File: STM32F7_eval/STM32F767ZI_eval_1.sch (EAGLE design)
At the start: 101 parts, among them CN3 GROVE-4P-CONN-I2C-90D, CN4 GROVE-4P-CONN-AN01-90D, CN5 ARDUINO_COMPAT_IF, CN6 STLINKV21_SWD_IF, CN7 WFT0750CZ09-SMD_, CN8 MCO_IF, CN9 UART_IF, Q1 PMF370XN_, SW1 SKRPACE010_, SW2 SKRPACE010_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

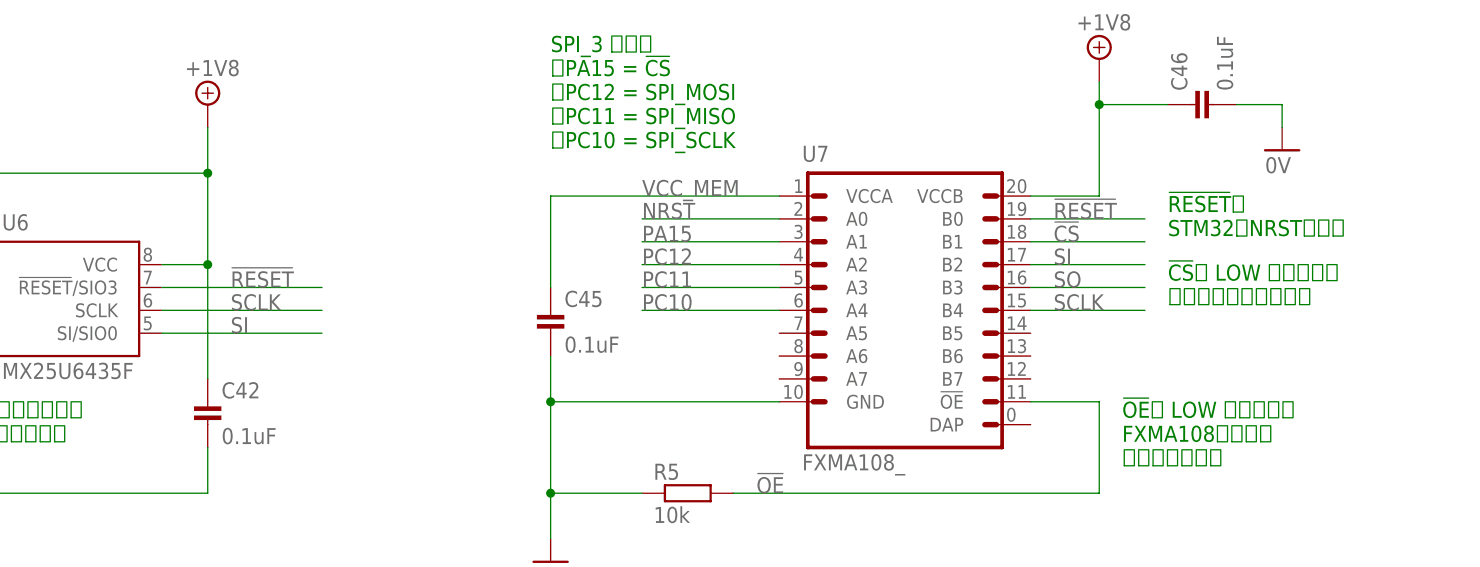
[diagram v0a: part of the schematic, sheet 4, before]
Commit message: 評価回路を修正
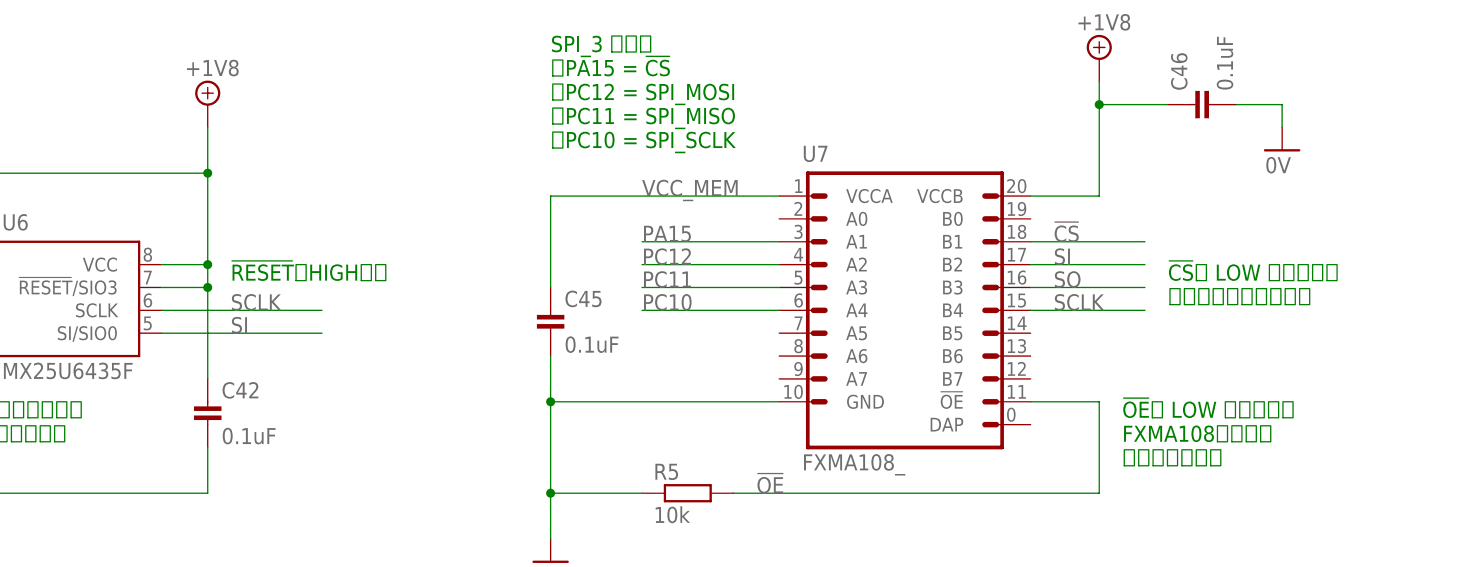
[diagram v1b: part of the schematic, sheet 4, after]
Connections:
- removed net !RESET!: U6.!RESET!/SIO3, U7.B0
- new net PE15: U1.PE15, U5.!RESET!
- net +1V8: now also U6.!RESET!/SIO3
- net NRST: no longer U5.!RESET!, U7.A0
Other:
- note added: "!RESET!はHIGH固定"
- note removed: "!RESET!は STM32のNRSTに接続"
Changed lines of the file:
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@@
 <setting verticaltext="up"/>
 </settings>
-<grid distance="0.1" unitdist="inch" unit="inch" style="lines" multiple="1" display="no" altdistance="0.01" altunitdist="inch" altunit="inch"/>
+<grid distance="0.1" unitdist="inch" unit="inch" style="lines" multiple="1" display="yes" altdistance="0.01" altunitdist="inch" altunit="inch"/>
 <layers>
 <layer number="1" name="Top" color="4" fill="1" visible="no" active="no"/>
@@
 <net name="NRST" class="0">
 <segment>
-<pinref part="U1" gate="G$1" pin="NRST"/>
-<wire x1="129.54" y1="139.7" x2="119.38" y2="139.7" width="0.1524" layer="91"/>
-<label x="121.92" y="139.7" size="1.778" layer="95"/>
-</segment>
-<segment>
 <pinref part="C17" gate="G$1" pin="1"/>
 <wire x1="232.41" y1="35.56" x2="226.06" y2="35.56" width="0.1524" layer="91"/>
@@
 <junction x="226.06" y="45.72"/>
 <label x="215.9" y="45.72" size="1.778" layer="95"/>
+</segment>
+<segment>
+<pinref part="U1" gate="G$1" pin="NRST"/>
+<wire x1="129.54" y1="139.7" x2="119.38" y2="139.7" width="0.1524" layer="91"/>
+<label x="121.92" y="139.7" size="1.778" layer="95"/>
 </segment>
 </net>
@@
 <wire x1="22.86" y1="142.24" x2="22.86" y2="154.94" width="0.1524" layer="91"/>
 <label x="22.86" y="144.78" size="1.778" layer="95" rot="R90"/>
+</segment>
+</net>
+<net name="PE15" class="0">
+<segment>
+<pinref part="U1" gate="G$1" pin="PE15"/>
+<wire x1="226.06" y1="93.98" x2="226.06" y2="83.82" width="0.1524" layer="91"/>
+<label x="226.06" y="86.36" size="1.778" layer="95" rot="R90"/>
 </segment>
 </net>
@@
 </segment>
 </net>
-<net name="NRST" class="0">
-<segment>
-<pinref part="U5" gate="G$1" pin="!RESET!"/>
-<wire x1="76.2" y1="33.02" x2="60.96" y2="33.02" width="0.1524" layer="91"/>
-<label x="63.5" y="33.02" size="1.778" layer="95"/>
-</segment>
-</net>
 <net name="PB10" class="0">
 <segment>
@@
 </segment>
 </net>
+<net name="PE15" class="0">
+<segment>
+<pinref part="U5" gate="G$1" pin="!RESET!"/>
+<wire x1="76.2" y1="33.02" x2="60.96" y2="33.02" width="0.1524" layer="91"/>
+<label x="63.5" y="33.02" size="1.778" layer="95"/>
+</segment>
+</net>
 </nets>
 </sheet>
@@
 <text x="200.66" y="76.2" size="1.778" layer="91" align="top-left">!CS!に LOW を出力時は
 フラッシュが使用可能</text>
-<text x="200.66" y="83.82" size="1.778" layer="91" align="top-left">!RESET!は
-STM32のNRSTに接続</text>
+<text x="96.52" y="76.2" size="1.778" layer="91" align="top-left">!RESET!はHIGH固定</text>
 <text x="195.58" y="60.96" size="1.778" layer="91" align="top-left">!OE!に LOW を出力時は
 FXMA108のバスが
@@
 </segment>
 </net>
-<net name="!RESET!" class="0">
-<segment>
-<pinref part="U7" gate="G$1" pin="B0"/>
-<wire x1="185.42" y1="81.28" x2="198.12" y2="81.28" width="0.1524" layer="91"/>
-<label x="187.96" y="81.28" size="1.778" layer="95"/>
-</segment>
-<segment>
-<pinref part="U6" gate="G$1" pin="!RESET!/SIO3"/>
-<wire x1="106.68" y1="73.66" x2="88.9" y2="73.66" width="0.1524" layer="91"/>
-<label x="96.52" y="73.66" size="1.778" layer="95"/>
-</segment>
-</net>
 <net name="!CS!" class="0">
 <segment>
@@
 <wire x1="106.68" y1="71.12" x2="88.9" y2="71.12" width="0.1524" layer="91"/>
 <label x="96.52" y="71.12" size="1.778" layer="95"/>
-</segment>
-</net>
-<net name="NRST" class="0">
-<segment>
-<pinref part="U7" gate="G$1" pin="A0"/>
-<wire x1="157.48" y1="81.28" x2="142.24" y2="81.28" width="0.1524" layer="91"/>
-<label x="142.24" y="81.28" size="1.778" layer="95"/>
 </segment>
 </net>
@@
 <pinref part="C42" gate="G$1" pin="1"/>
 <wire x1="93.98" y1="86.36" x2="93.98" y2="91.44" width="0.1524" layer="91"/>
-<wire x1="93.98" y1="76.2" x2="93.98" y2="63.5" width="0.1524" layer="91"/>
+<wire x1="93.98" y1="76.2" x2="93.98" y2="73.66" width="0.1524" layer="91"/>
 <junction x="93.98" y="76.2"/>
 <pinref part="SUPPLY1" gate="G$1" pin="+1V8"/>
 <pinref part="U6" gate="G$1" pin="!WP!/SIO2"/>
+<wire x1="93.98" y1="73.66" x2="93.98" y2="63.5" width="0.1524" layer="91"/>
 <wire x1="55.88" y1="71.12" x2="43.18" y2="71.12" width="0.1524" layer="91"/>
 <wire x1="43.18" y1="71.12" x2="43.18" y2="86.36" width="0.1524" layer="91"/>
 <wire x1="43.18" y1="86.36" x2="93.98" y2="86.36" width="0.1524" layer="91"/>
 <junction x="93.98" y="86.36"/>
-</segment>
-<segment>
+<pinref part="U6" gate="G$1" pin="!RESET!/SIO3"/>
+<wire x1="88.9" y1="73.66" x2="93.98" y2="73.66" width="0.1524" layer="91"/>
+<junction x="93.98" y="73.66"/>
+</segment>
+<segment>

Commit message: 回路図を修正
・部品のパッケージを入れ替え
・セキュリティーチップ回路図のシートを移動
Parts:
- removed C28: 0.1uF, Parts:CAP_0603_DEV
- removed C29: 10uF, Parts:CAP_0805_DEV
- removed CN8: MCO_IF, PartsForProto:MCO_IF
- removed R19, R20: 3.3k, Parts:RESISTOR_0603_DEV
- removed R26: 0, Parts:RESISTOR_0603_DEV
- removed U5: STSAFE, Parts:STSAFE
- added C47: 0.1uF, Parts:CAP_0603_DEV
- added C48: 10uF, Parts:CAP_0805_DEV
- added R27, R28: 3.3k, Parts:RESISTOR_0603_DEV
- added R29: 0, Parts:RESISTOR_0603_DEV
- added U9: STSAFE, Parts:STSAFE
- CN4: value GROVE-4P-CONN-AN01-90D -> GROVE-4P-CONN-I2C-90D; device PartsForProto:GROVE-4P-CONN-AN01-90D -> PartsForProto:GROVE-4P-CONN-I2C-90D
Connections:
- net 0V: now also C47.2, C48.2, CN4.GND, U9.GND; no longer C28.2, C29.2, U5.GND
- net AGND: no longer CN4.GND
- net AVDD: no longer CN4.VCC
- net PA3: no longer CN4.A0
- net PB10: now also R27.1, U9.SCL; no longer R19.1, U5.SCL
- net PB11: now also R28.1, U9.SDA; no longer R20.1, U5.SDA
- net PB8: now also CN4.SCL
- net PB9: now also CN4.SDA
- net PC0: no longer CN4.A1
- net PE15: now also U9.!RESET!; no longer U5.!RESET!
- net PH0: no longer CN8.MCO
- net VCC_STSAFE: now also C47.1, C48.1, R27.2, R28.2, R29.1, U9.VCC; no longer C28.1, C29.1, R19.2, R20.2, R26.1, U5.VCC
- net VDD: now also CN4.VCC, R29.2; no longer R26.2
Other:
- note added: "Groveコネクター ・I2Cポート x 2"
- note added: "実装していません"
- note removed: "Groveコネクター ・I2Cポート ・アナログポート"
- note removed: "ST-LINK V2-1からの マスタークロック入力ピン"

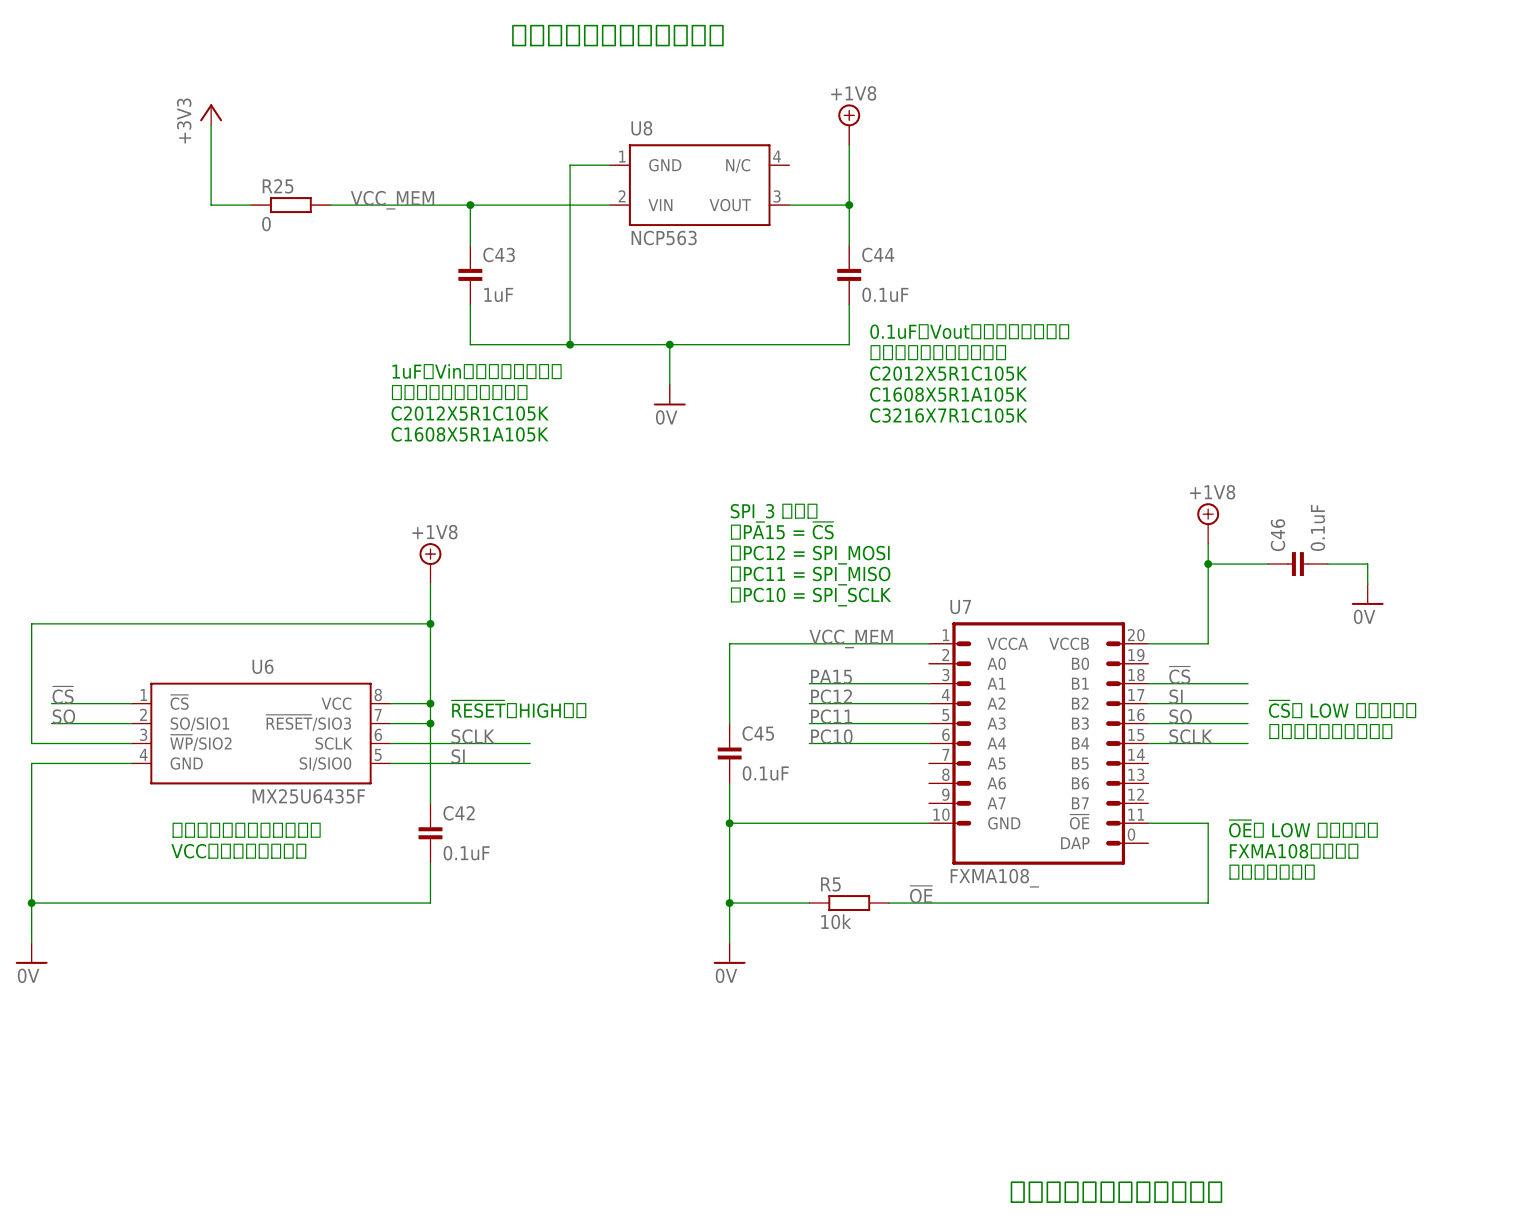
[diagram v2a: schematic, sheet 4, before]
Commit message: 回路図を修正
・構成部品を入替え
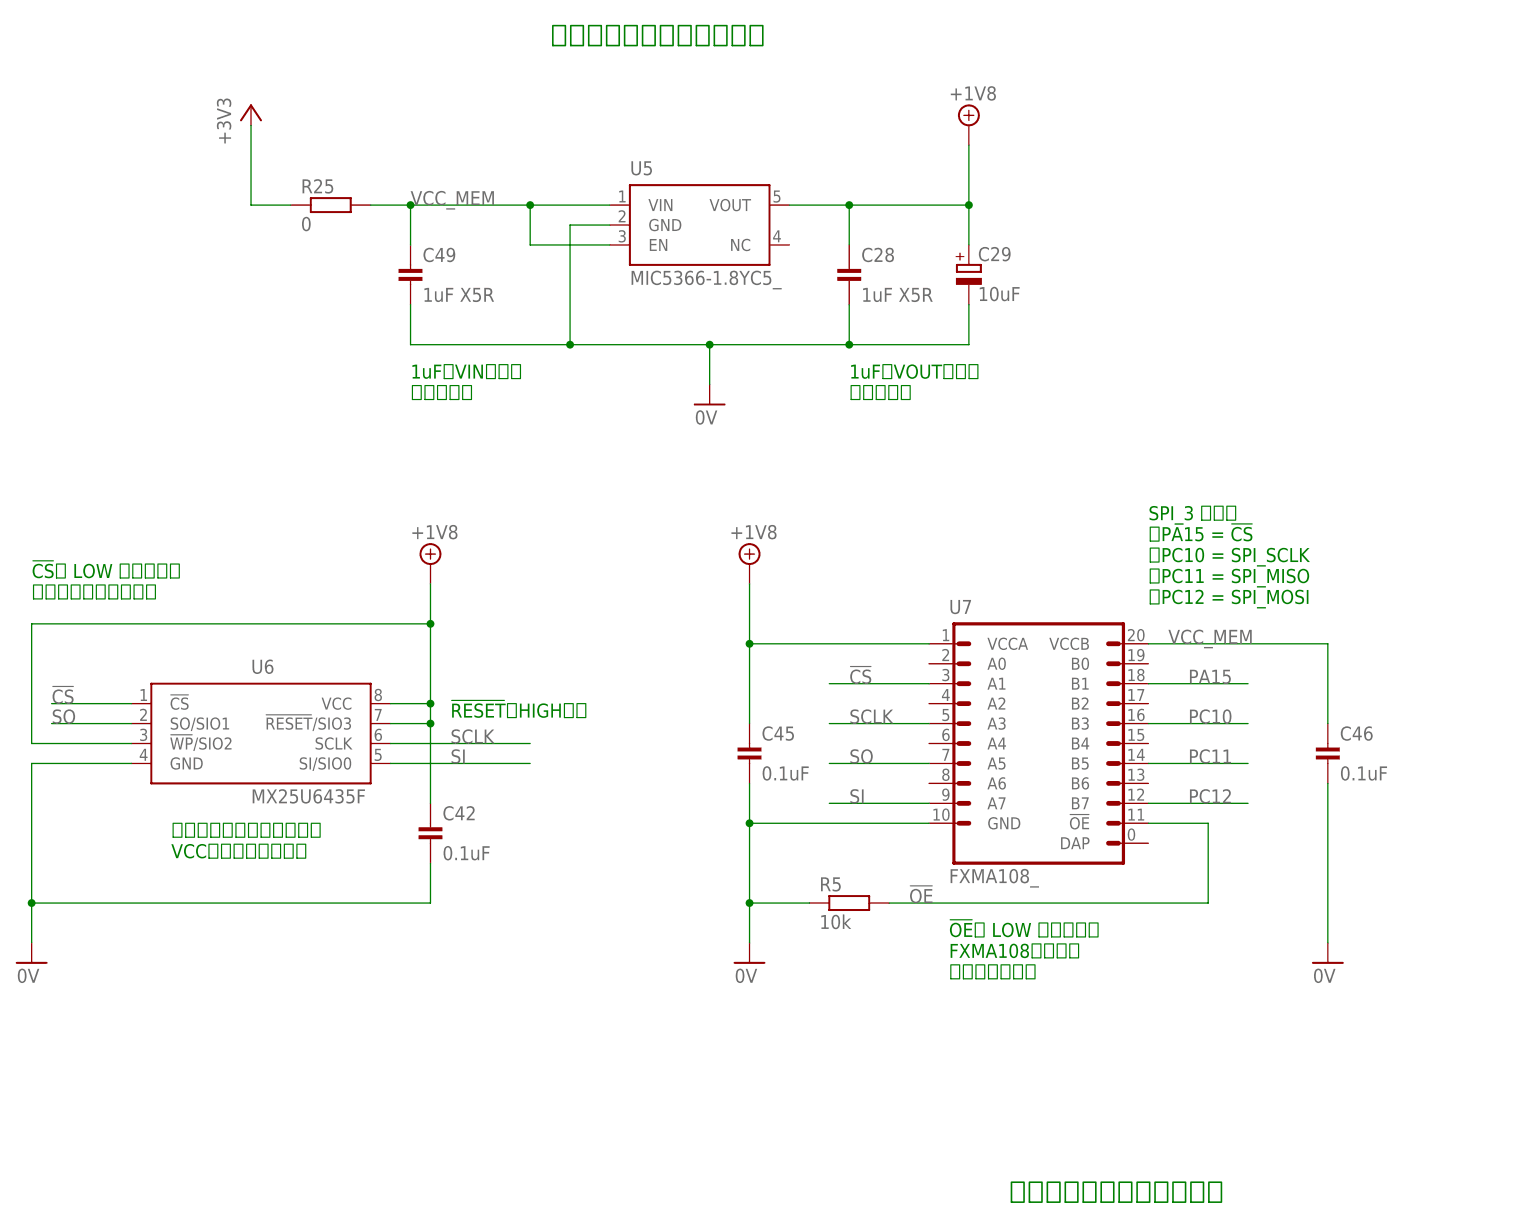
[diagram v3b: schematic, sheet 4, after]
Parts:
- removed C43: 1uF, Parts:CAP_0603_DEV
- removed U8: NCP563, Parts:NCP563
- added C29: 10uF, Parts:TPST106K016R0800_
- added C49: 1uF X5R, Parts:CAP_0603_DEV
- added U5: MIC5366-1.8YC5_, Parts:MIC5366-1.8YC5_
- C28: value 0.1uF -> 1uF X5R
- renumbered C44 to C28
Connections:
- net !CS!: now also U7.A1; no longer U7.B1
- net +1V8: now also C29.+, C45.1, U5.VOUT, U7.VCCA; no longer C46.1, U7.VCCB, U8.VOUT
- net 0V: now also C29.-, C49.2, U5.GND; no longer C43.2, U8.GND
- net PA15: now also U7.B1; no longer U7.A1
- net PC10: now also U7.B3; no longer U7.A4
- net PC11: now also U7.B5; no longer U7.A3
- net PC12: now also U7.B7; no longer U7.A2
- net SCLK: now also U7.A3; no longer U7.B4
- net SI: now also U7.A7; no longer U7.B2
- net SO: now also U7.A5; no longer U7.B3
- net VCC_MEM: now also C46.1, C49.1, U5.EN, U5.VIN, U7.VCCB; no longer C43.1, C45.1, U7.VCCA, U8.VIN
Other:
- note added: "1uFはVINピンの 近傍に設置"
- note added: "1uFはVOUTピンの 近傍に設置"
- note added: "SPI_3 を使用 ・PA15 = !CS! ・PC10 = SPI_SCLK ・PC11 = SPI_MISO ・PC12 = SPI_MOSI"
- note removed: "0.1uFをVoutピンの近傍に設置 以下のいずれかを推奨： C2012X5R1C105K C1608X5R1A105K C3216X7R1C105K"
- note removed: "1uFをVinピンの近傍に設置 以下のいずれかを推奨： C2012X5R1C105K C1608X5R1A105K"
- note removed: "SPI_3 を使用 ・PA15 = !CS! ・PC12 = SPI_MOSI ・PC11 = SPI_MISO ・PC10 = SPI_SCLK"
- moved on the sheet: C45, C46, R25
